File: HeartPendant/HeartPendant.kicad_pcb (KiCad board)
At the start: 4 copper layers, 108 x 104.2 mm, 82 parts, among them J1 Bat, J2 USB_C_Receptacle_USB2.0_16P, J3 Bat, J4 USB_C_Receptacle_USB2.0_16P, Q1 2N7002, Q2 AO3401A, SW1 SW_Boot, SW2 SW_SPDT, SW3 SW_Boot, SW4 SW_SPDT, U1 MCP73831-2-OT, U2 ESP32-C3-MINI-1-N4X, U3 MAX30102_Module, U4 AP2112K-3.3, U5 USBLC6-2SC6, U6 MCP73831-2-OT, U7 ESP32-C3-MINI-1-N4X, U8 USBLC6-2SC6, U9 AP2112K-3.3

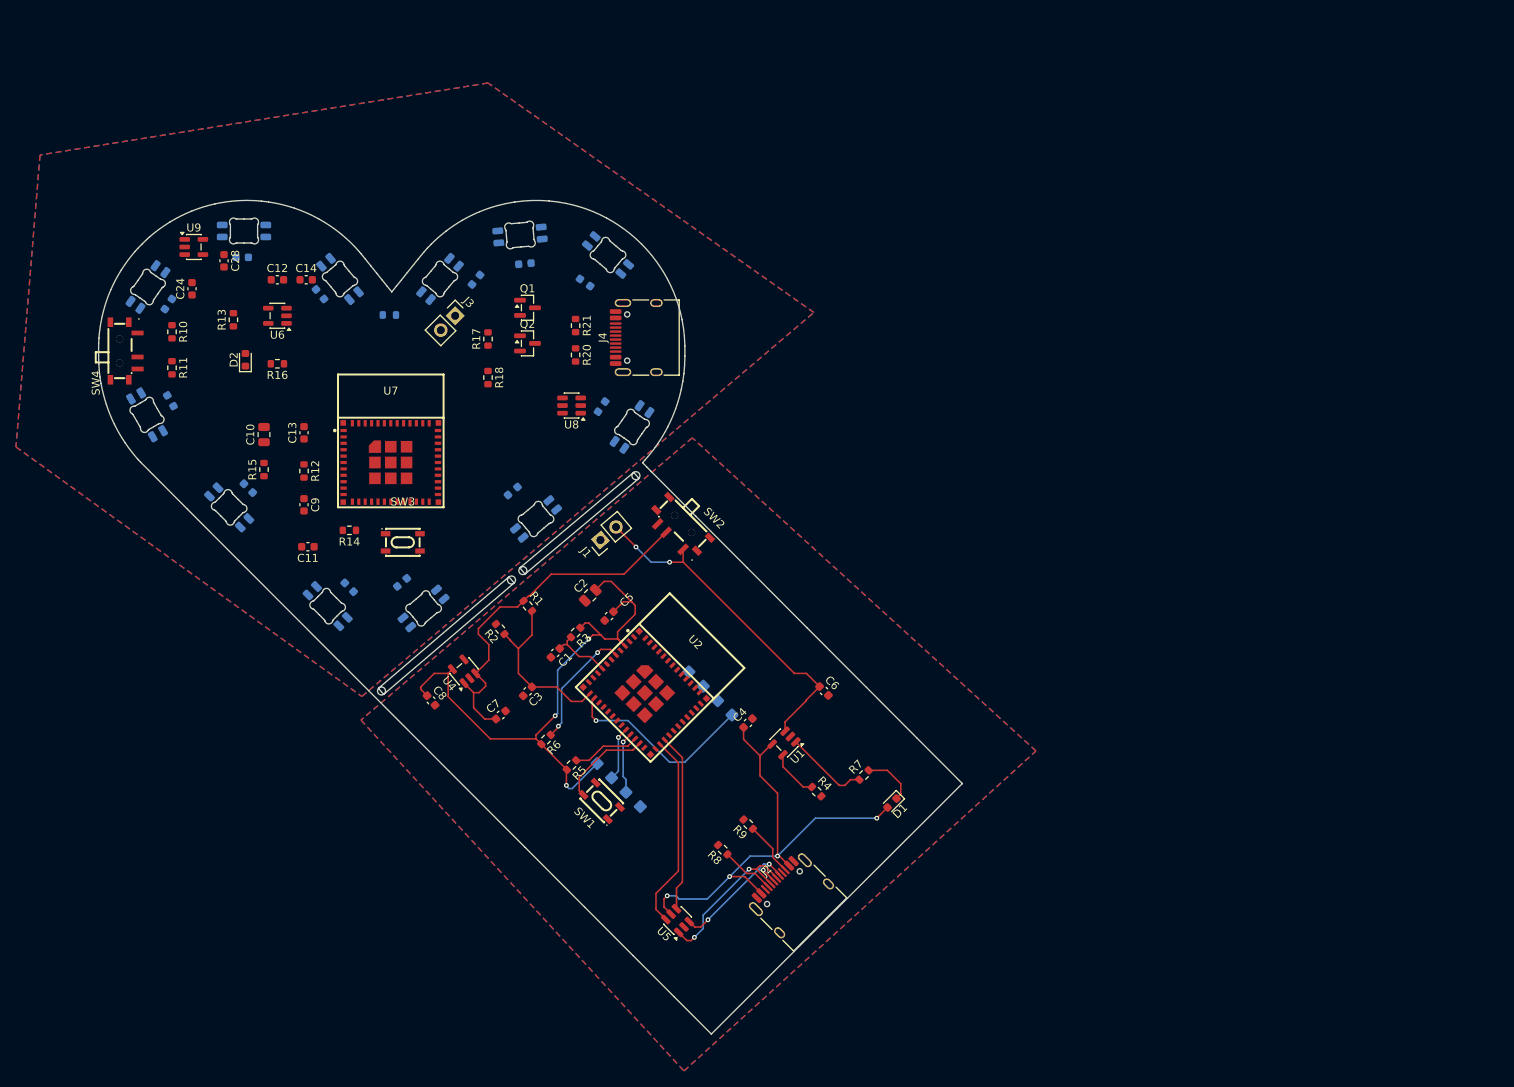
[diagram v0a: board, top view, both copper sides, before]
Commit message: Finished pendant routing, added production files
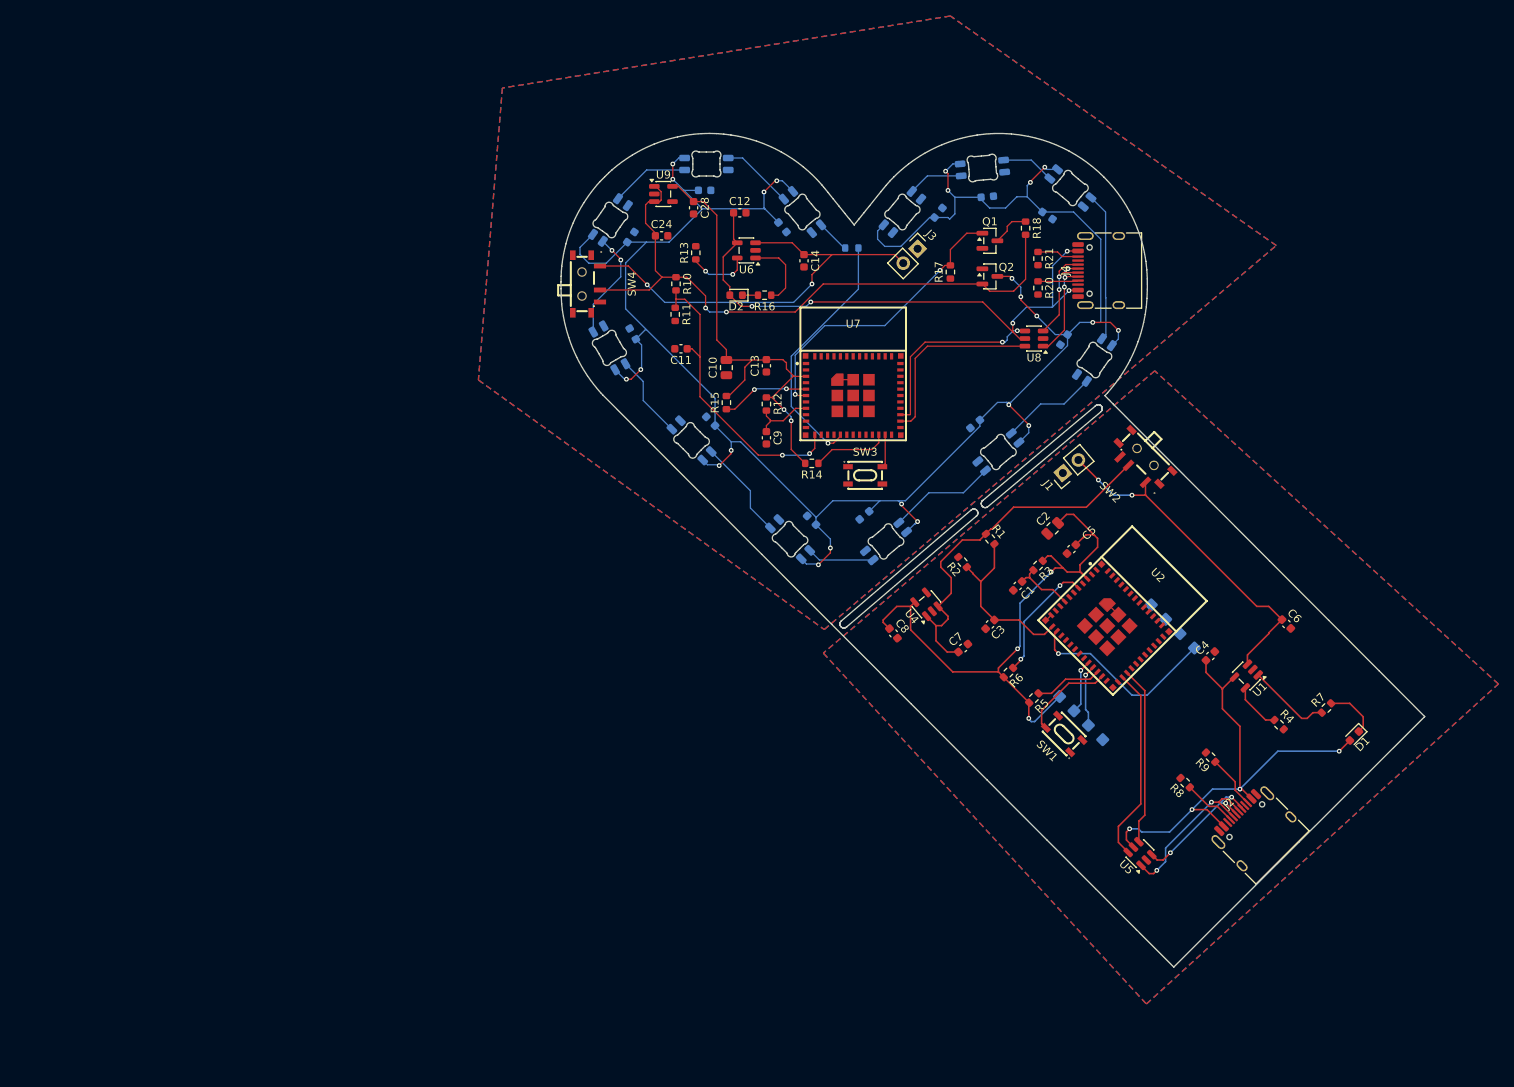
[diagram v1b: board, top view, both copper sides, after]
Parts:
- moved R18 69.7 mm to (167.7, 51.7)
- moved R10 63.3 mm to (124.0, 58.6)
- moved R11 63.3 mm to (123.9, 62.4)
- moved C14 62.3 mm to (140.0, 55.7), turned to -90 degrees
- moved D2 61.9 mm to (131.5, 60.0), turned to 180 degrees
- moved R16 61.5 mm to (135.1, 60.0)
- moved U6 59.2 mm to (132.8, 54.4)
- moved C24 59.1 mm to (122.2, 52.6), turned to 0 degrees
- moved C28 59.1 mm to (126.2, 49.1)
- moved U9 59.1 mm to (122.4, 47.4)
- moved R8 58.4 mm to (187.6, 121.0)
- moved C10 58.4 mm to (130.3, 69.1)
- moved C13 58.4 mm to (135.3, 68.9)
- moved C15 58.4 mm to (137.3, 51.5)
- moved C20 58.4 mm to (161.4, 76.1)
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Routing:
- net /Pendant/LED_VDD: track 0.00 -> 261.6 mm, vias 0 -> 23
- net /Pendant/VBAT_SW: track 0.00 -> 78.8 mm, vias 0 -> 2
- net /Pendant/VBUS: track 0.00 -> 71.4 mm, vias 0 -> 5
- net +3V3_P: track 0.00 -> 57.4 mm, vias 0 -> 2
- net /Pendant/VBAT: track 0.00 -> 53.6 mm, vias 0 -> 2
- net /Pendant/VBAT_SENSE: track 0.00 -> 37.8 mm, vias 0 -> 2
- net /Pendant/LED_SW: track 0.00 -> 37.2 mm, vias 0 -> 2
- net /Pendant/LED_DATA: track 0.00 -> 31.9 mm, vias 0 -> 1
- net /Pendant/D+: track 0.00 -> 24.4 mm, vias 0 -> 2
- net /Pendant/D-: track 0.00 -> 23.7 mm
- net /Pendant/D_3: track 0.00 -> 18.6 mm
- net Net-(J4-D--PadA7): track 0.00 -> 14.3 mm, vias 0 -> 3
- net /Pendant/D_1: track 0.00 -> 13.7 mm, vias 0 -> 2
- net Net-(J4-D+-PadA6): track 0.00 -> 13.6 mm, vias 0 -> 2
- net Net-(D5-DOUT): track 0.00 -> 13.5 mm
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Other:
- outline, holes or cut-outs redrawn
- copper layers 4 -> 2
- board text added: "Made by Rayan Berrabah :)"
